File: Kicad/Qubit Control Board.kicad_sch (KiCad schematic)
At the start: 65 parts, among them J1 USB_C_Receptacle_PowerOnly_6P, J2 CLK_Pins, J3 Idata, J4 Qdata, U1 TRF372017IRGZR, U3 LT1963AxST-3.3, U4 LT1963AxST-1.8, U5 SN65LVDS1DBV, U6 AD9743BCPZ

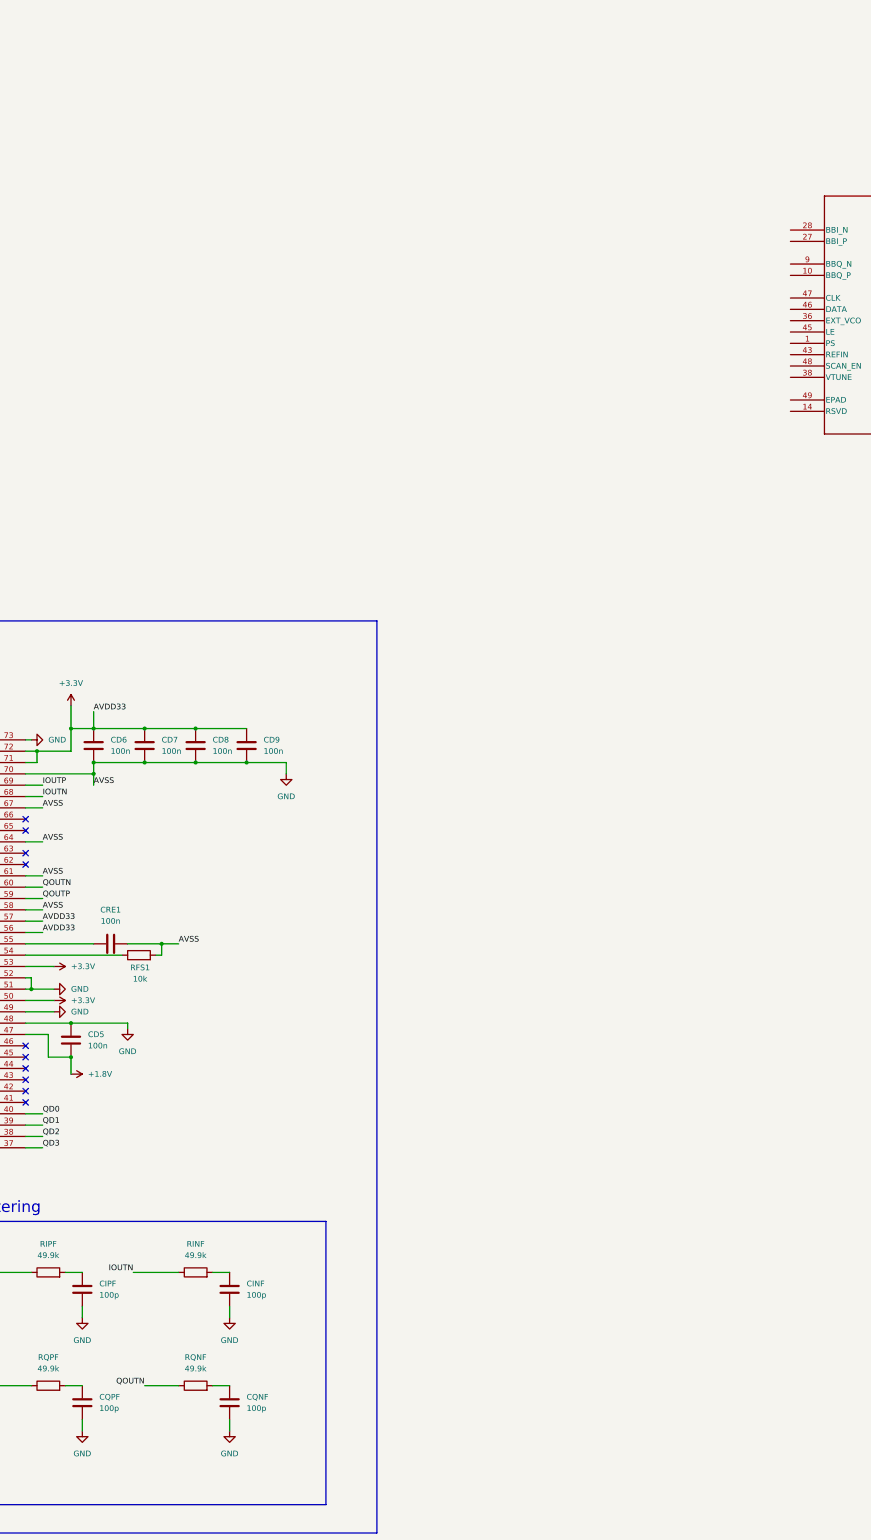
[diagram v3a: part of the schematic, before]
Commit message: started on IQ mixer and added oscillator
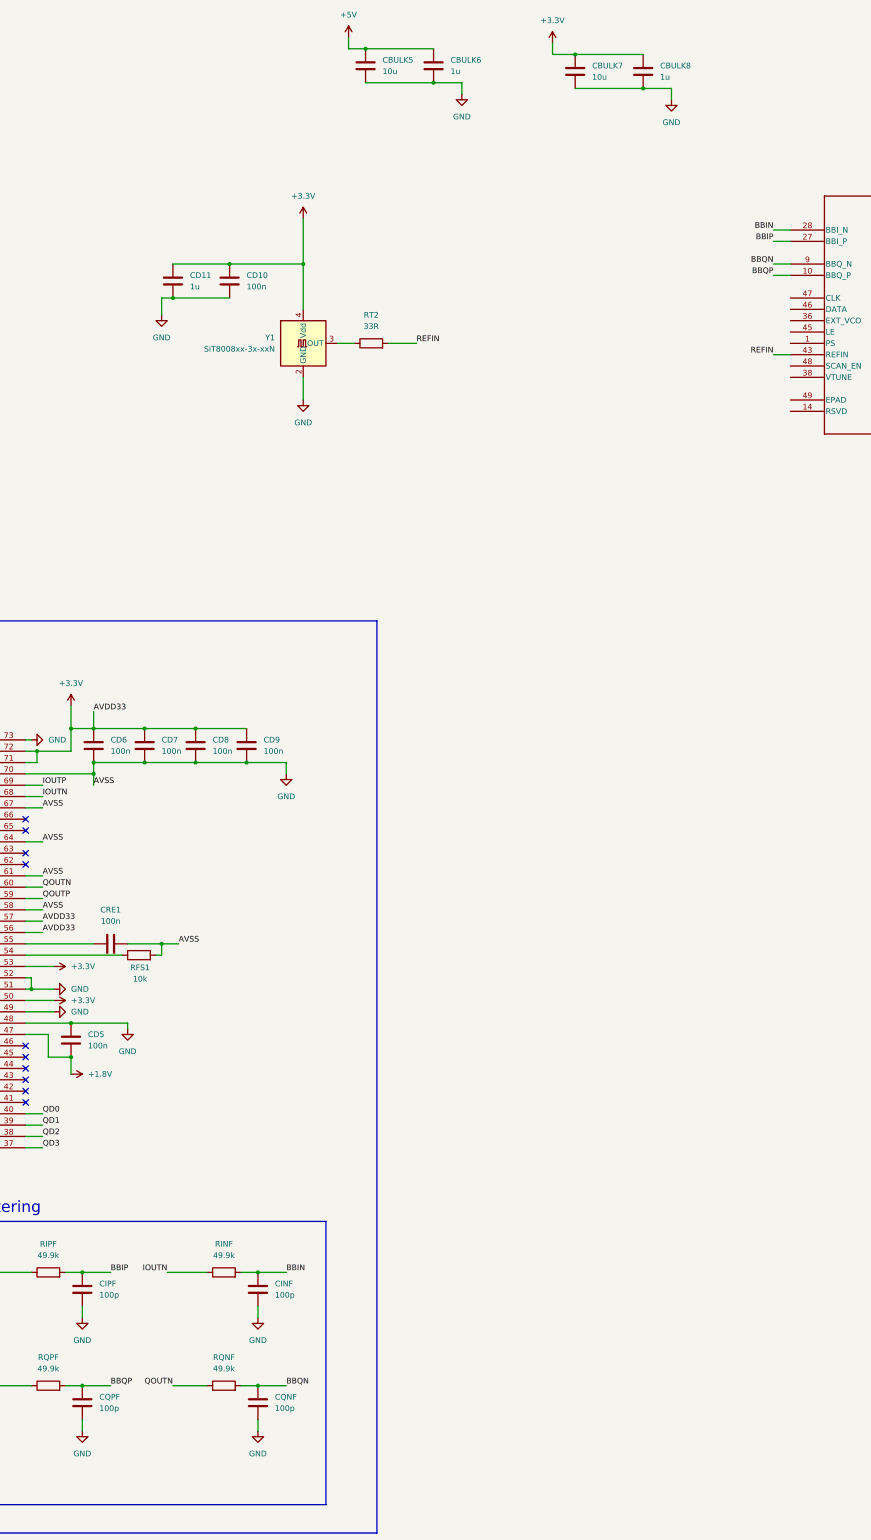
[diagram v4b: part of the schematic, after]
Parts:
- added CBULK5, CBULK7: 10u, symbol Device:C
- added CBULK6, CBULK8, CD11: 1u, symbol Device:C
- added CD10: 100n, symbol Device:C
- added RT2: 33R, symbol Device:R
- added Y1: SiT8008xx-3x-xxN, Oscillator:Oscillator_SMD_SiT_PQFN-4Pin_5.0x3.2mm, symbol Oscillator:SiT8008xx-3x-xxN
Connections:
- net +3.3V: now also CBULK7.1, CBULK8.1, CD10.2, CD11.2, Y1.4 (Vdd)
- net +5V: now also CBULK5.1, CBULK6.1
- net GND: now also CBULK5.2, CBULK6.2, CBULK7.2, CBULK8.2, CD10.1, CD11.1, Y1.2 (GND)
- net BBIN: now reaches CINF.1, RINF.2
- net BBIN: now also U1.28 (BBI_N)
- net BBQN: now reaches CQNF.1, RQNF.2
- net BBQN: now also U1.9 (BBQ_N)
- net BBIP: now reaches CIPF.1, RIPF.2
- net BBIP: now also U1.27 (BBI_P)
- net BBQP: now reaches U1.10 (BBQ_P)
- net BBQP: now also CQPF.1, RQPF.2
- net REFIN: now reaches U1.43 (REFIN)
- net REFIN: now also RT2.2
- new net: RT2.1, Y1.3 (OUT)
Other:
- moved on the sheet: CINF, CQNF, RINF, RQNF

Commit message: VCO power input filtering
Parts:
- removed U1: TRF372017IRGZR, RGZ48_5P6X5P6, symbol TRF372017:TRF372017IRGZR
- added CCIN1, CCIP1, CCQN, CCQP: 100n, symbol Device:C
- added CD12, CD13, CD18, CD19, CD23, CD24, CD25: 4.7p, symbol Device:C
- added CD14, CD15, CD16, CD17, CD27: 100p, symbol Device:C
- added CD20, CD21, CD22, CD26: 1u, symbol Device:C
- added FB1, FB2, FB3, FB4: 1k @100MHz, symbol Device:FerriteBead
- added RDIFF2, RDIFF3: 100R, symbol Device:R
- added U2: TRF372017IRGZR, RGZ48_5P6X5P6, symbol TRF372017_:TRF372017IRGZR
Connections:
- net +3.3V: now also FB2.1, FB3.1, FB4.1
- net +5V: now also FB1.1
- net BBIN: now also CCIN1.1
- net BBIP: now also CCIP1.1
- net BBQN: now also CCQN.1
- net BBQP: now also CCQP.1
- net GND: now also CD12.1, CD13.1, CD14.1, CD15.1, CD16.1, CD17.1, CD18.1, CD19.1, CD20.1, CD21.1, CD22.1, CD23.1, CD24.1, CD25.1, CD26.1, CD27.1, U2.11 (GND), U2.12 (GND), U2.13 (GND), U2.15 (GND), U2.16 (GND), U2.17 (GND), U2.19 (GND), U2.22 (GND), U2.23 (GND), U2.24 (GND)
- new net: CD12.2, CD13.2, CD14.2, CD15.2, FB1.2, U2.20 (VCC_D2S), U2.21 (VCC_MIX)
- new net: CCQN.2, RDIFF3.1, U2.9 (BBQ_N)
- new net: CCQP.2, RDIFF3.2, U2.10 (BBQ_P)
- new net: CCIP1.2, RDIFF2.1, U2.27 (BBI_P)
- new net: CCIN1.2, RDIFF2.2, U2.28 (BBI_N)
- new net: U2.25 (GND), U2.26 (GND)
- new net RFOUT: U2.18 (RFOUT)
- new net VCC_DIG: CD26.2, CD27.2, FB4.2, U2.3 (VCC_DIG)
- new net VCC_LO1: CD16.2, CD17.2, CD18.2, CD19.2, FB2.2, U2.30 (VCC_LO2), U2.7 (VCC_LO1)
- new net VCC_PLL: CD20.2, CD21.2, CD22.2, CD23.2, CD24.2, CD25.2, FB3.2, U2.32 (VCC_VCO2), U2.35 (VCC_VCO1), U2.41 (VCC_PLL)
- no-connect marks 19 -> 25
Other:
- note added: "100 MHz"
- note added: "F_c = 31.895 MHz"

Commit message: Finished IQ modulator with PLL/VCO
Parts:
- added CC1: 47p, symbol Device:C
- added CC2: 22p, symbol Device:C
- added CLF1: 270p, symbol Device:C
- added CLF2, CLF3: 4.7n, symbol Device:C
- added J5: SPIdata, symbol Connector_Generic_MountingPin:Conn_01x06_MountingPin
- added J6: SMA, symbol Connector_Generic_Shielded:Conn_01x01_Shielded
- added RAP1: 0R, symbol Device:R
- added RAP2, RAP3: DNP, symbol Device:R
- added RLF1, RLF2: 1.5k, symbol Device:R
- added RPD1, RPD2, RPD3: 10k, symbol Device:R
- added RTSPI1, RTSPI2, RTSPI3, RTSPI4, RTSPI5: 33R, symbol Device:R
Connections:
- net GND: now also U2.1 (PS), U2.25 (GND), U2.26 (GND), U2.29 (GND), U2.31 (GND), U2.37 (GND), U2.39 (GND), U2.4 (GND_DIG), U2.42 (GND), U2.44 (GND), U2.48 (SCAN_EN), U2.49 (EPAD), U2.6 (GND_DIG), U2.8 (GND), CLF1.2, CLF3.2, J5.6 (Pin_6), J6.SH (Shield), RAP2.1, RAP3.1, RLF1.2, RPD1.1, RPD2.1, RPD3.1
- net REFIN: now also U2.43 (REFIN), CC1.2; no longer RT2.2
- net RFOUT: now also CC2.1
- net RDBK: now reaches U2.2 (RDBK)
- net RDBK: now also RTSPI5.1
- net VTUNE: now reaches U2.38 (VTUNE)
- net VTUNE: now also CLF3.1, RLF2.2
- net CP_OUT: now reaches U2.40 (CP_OUT)
- net CP_OUT: now also CLF1.1, CLF2.1, RLF2.1
- net LE: now reaches U2.45 (LE)
- net LE: now also RPD3.2, RTSPI1.1
- net DATA: now reaches U2.46 (DATA)
- net DATA: now also RPD2.2, RTSPI2.1
- net CLK: now reaches U2.47 (CLK)
- net CLK: now also RPD1.2, RTSPI3.1
- net LD: now reaches U2.5 (LD)
- net LD: now also RTSPI4.1
- new net: J5.2 (Pin_2), RTSPI4.2
- new net: CC2.2, RAP1.1, RAP2.2
- new net: CC1.1, RT2.2
- new net: CLF2.2, RLF1.1
- new net: J5.1 (Pin_1), RTSPI5.2
- new net: J6.1 (Pin_1), RAP1.2, RAP3.2
- new net: J5.5 (Pin_5), RTSPI1.2
- new net: J5.3 (Pin_3), RTSPI3.2
- new net: J5.4 (Pin_4), RTSPI2.2
- no-connect marks 25 -> 26
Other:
- note added: "Differential Clock Buffer"
- note added: "IQ Data Pin Header"
- note added: "IQ Modulator PLL/VCO"
- note added: "Loop Filter"
- note added: "PLL Clock"
- note added: "Power Filtering"
- note added: "SMA Output"
- note added: "SPI Pin Header"
- moved on the sheet: CBULK5, CBULK6, CBULK7, CBULK8, CCIN1, CCIP1, CCQN, CCQP, CD10, CD11, CD12, CD13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

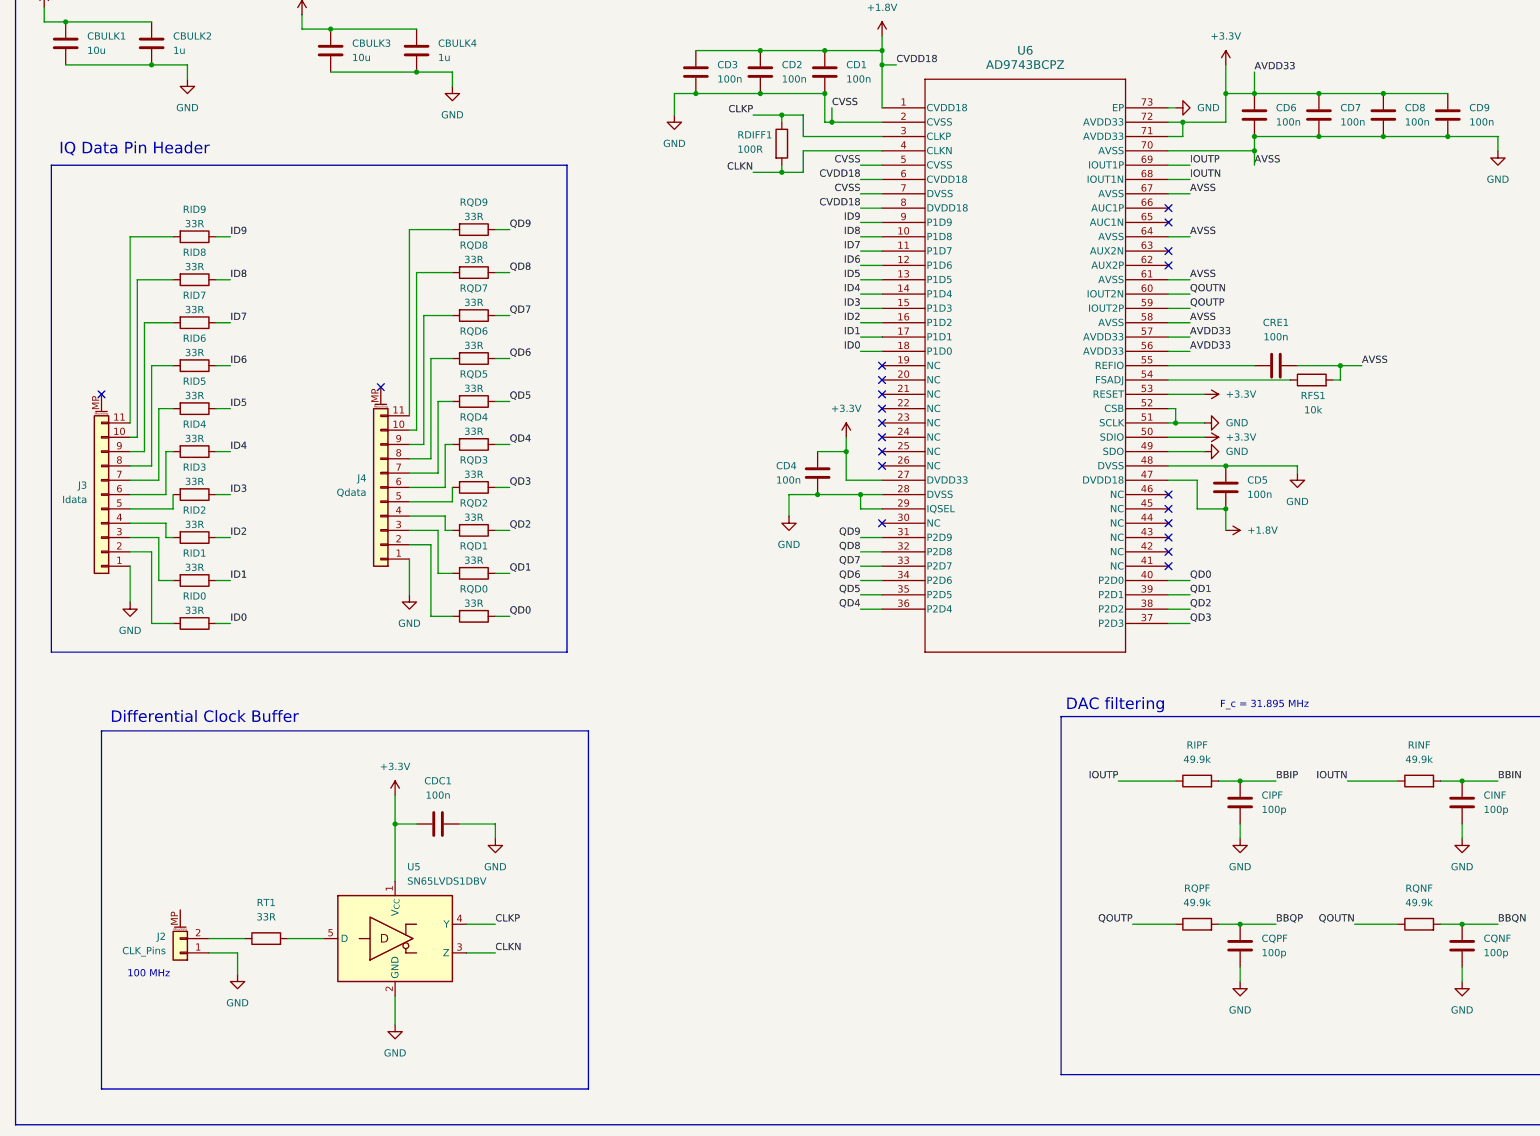
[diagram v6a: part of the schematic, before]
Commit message: DAC clock changed and RC filter changes
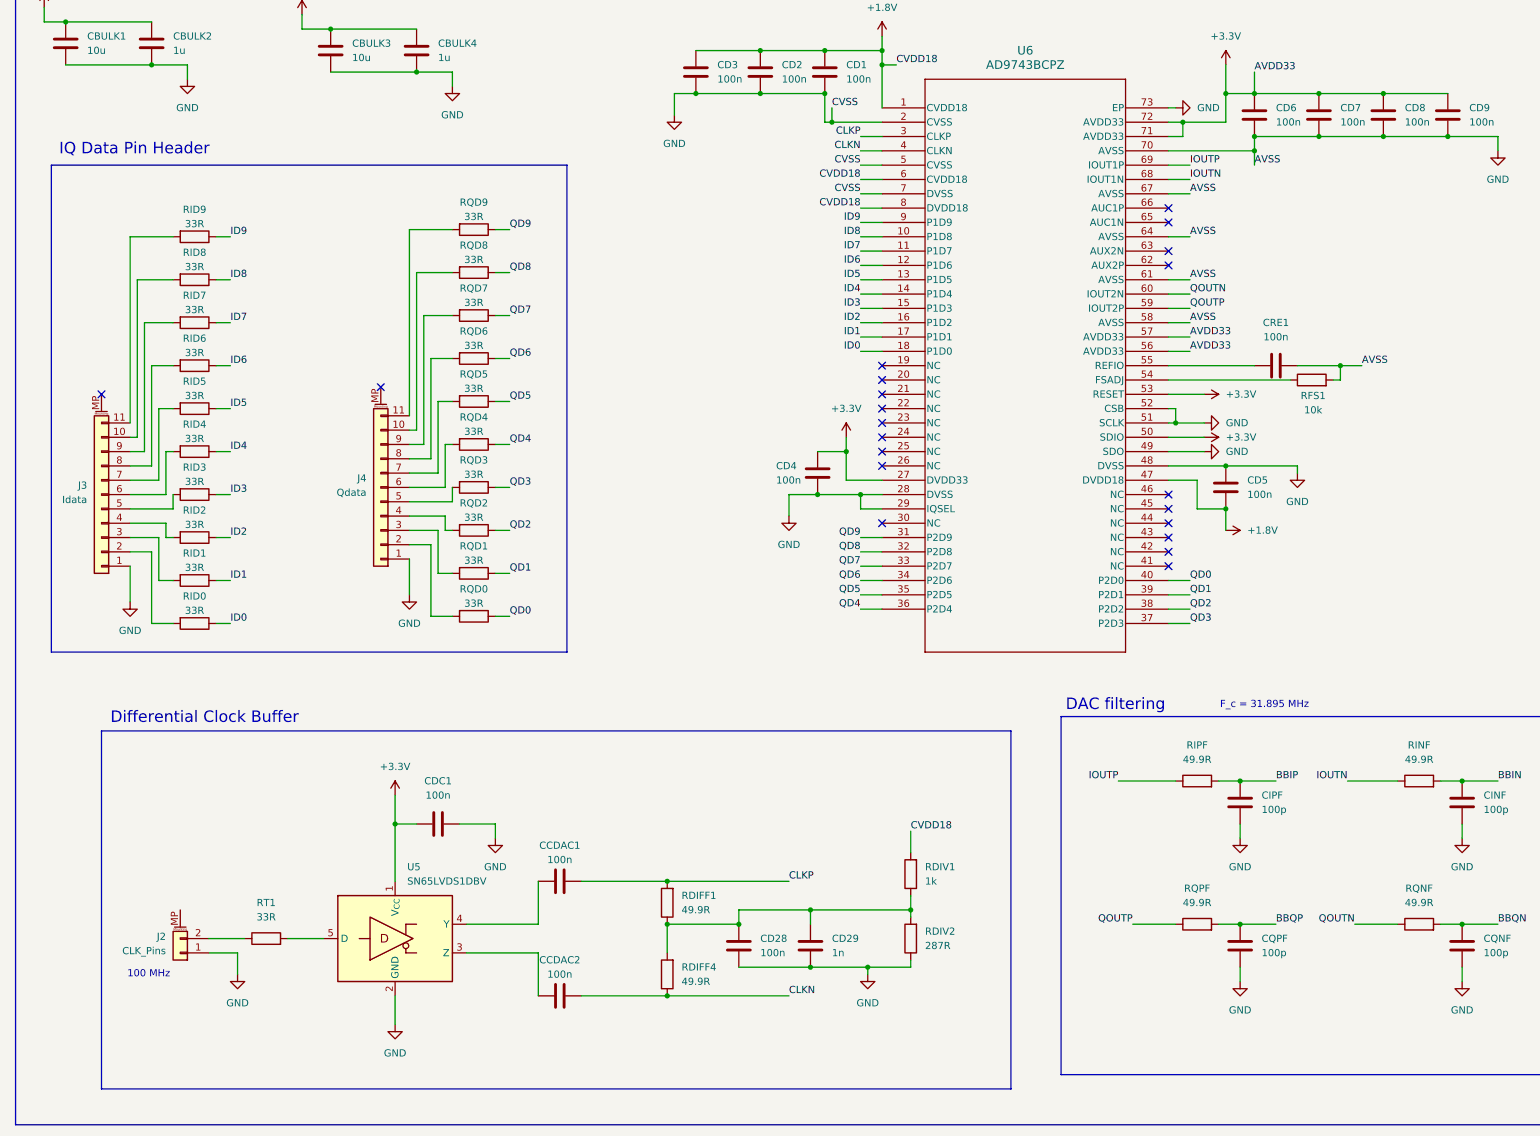
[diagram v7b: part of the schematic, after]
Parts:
- added CCDAC1, CCDAC2, CD28: 100n, symbol Device:C
- added CD29: 1n, symbol Device:C
- added RDIFF4: 49.9R, symbol Device:R
- added RDIV1: 1k, symbol Device:R
- added RDIV2: 287R, symbol Device:R
- RDIFF1: value 100R -> 49.9R
- RINF, RIPF, RQNF, RQPF: value 49.9k -> 49.9R
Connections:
- net +1.8V: now also RDIV1.2
- net CLKN: now also CCDAC2.2, RDIFF4.1; no longer RDIFF1.2, U5.3 (Z)
- net CLKP: now also RDIFF1.2, CCDAC1.2; no longer RDIFF1.1, U5.4 (Y)
- net GND: now also CD28.1, CD29.1, RDIV2.1
- new net: CD28.2, CD29.2, RDIFF1.1, RDIFF4.2, RDIV1.1, RDIV2.2
- new net: CCDAC2.1, U5.3 (Z)
- new net: CCDAC1.1, U5.4 (Y)
